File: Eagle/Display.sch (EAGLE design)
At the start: 79 parts, among them Q0A 310mA/60V/1.6Ω, Q0B 310mA/60V/1.6Ω, Q0C 310mA/60V/1.6Ω, Q10 310mA/60V/1.6Ω, Q11 310mA/60V/1.6Ω, Q12 310mA/60V/1.6Ω, Q13 310mA/60V/1.6Ω, Q14 310mA/60V/1.6Ω, Q15 310mA/60V/1.6Ω, Q16 310mA/60V/1.6Ω, Q17 310mA/60V/1.6Ω, Q18 310mA/60V/1.6Ω, Q19 310mA/60V/1.6Ω, Q1A 310mA/60V/1.6Ω, Q1B 310mA/60V/1.6Ω, Q1C 310mA/60V/1.6Ω, Q20 310mA/60V/1.6Ω, Q21 310mA/60V/1.6Ω, Q22A 310mA/60V/1.6Ω, Q22B 310mA/60V/1.6Ω, Q22C 310mA/60V/1.6Ω, Q22D 310mA/60V/1.6Ω, Q23 310mA/60V/1.6Ω, Q24 310mA/60V/1.6Ω, Q25 310mA/60V/1.6Ω, Q26 310mA/60V/1.6Ω, Q2A 310mA/60V/1.6Ω, Q2B 310mA/60V/1.6Ω, Q2C 310mA/60V/1.6Ω, Q3A 310mA/60V/1.6Ω, Q3B 310mA/60V/1.6Ω, Q3C 310mA/60V/1.6Ω, Q4A 310mA/60V/1.6Ω, Q4B 310mA/60V/1.6Ω, Q4C 310mA/60V/1.6Ω, Q5A 310mA/60V/1.6Ω, Q5B 310mA/60V/1.6Ω, Q5C 310mA/60V/1.6Ω, Q6A 310mA/60V/1.6Ω, Q6B 310mA/60V/1.6Ω, Q6C 310mA/60V/1.6Ω, Q7A 310mA/60V/1.6Ω, Q7B 310mA/60V/1.6Ω, Q7C 310mA/60V/1.6Ω, Q8A 310mA/60V/1.6Ω, Q8B 310mA/60V/1.6Ω, Q8C 310mA/60V/1.6Ω, Q9A 310mA/60V/1.6Ω, Q9B 310mA/60V/1.6Ω

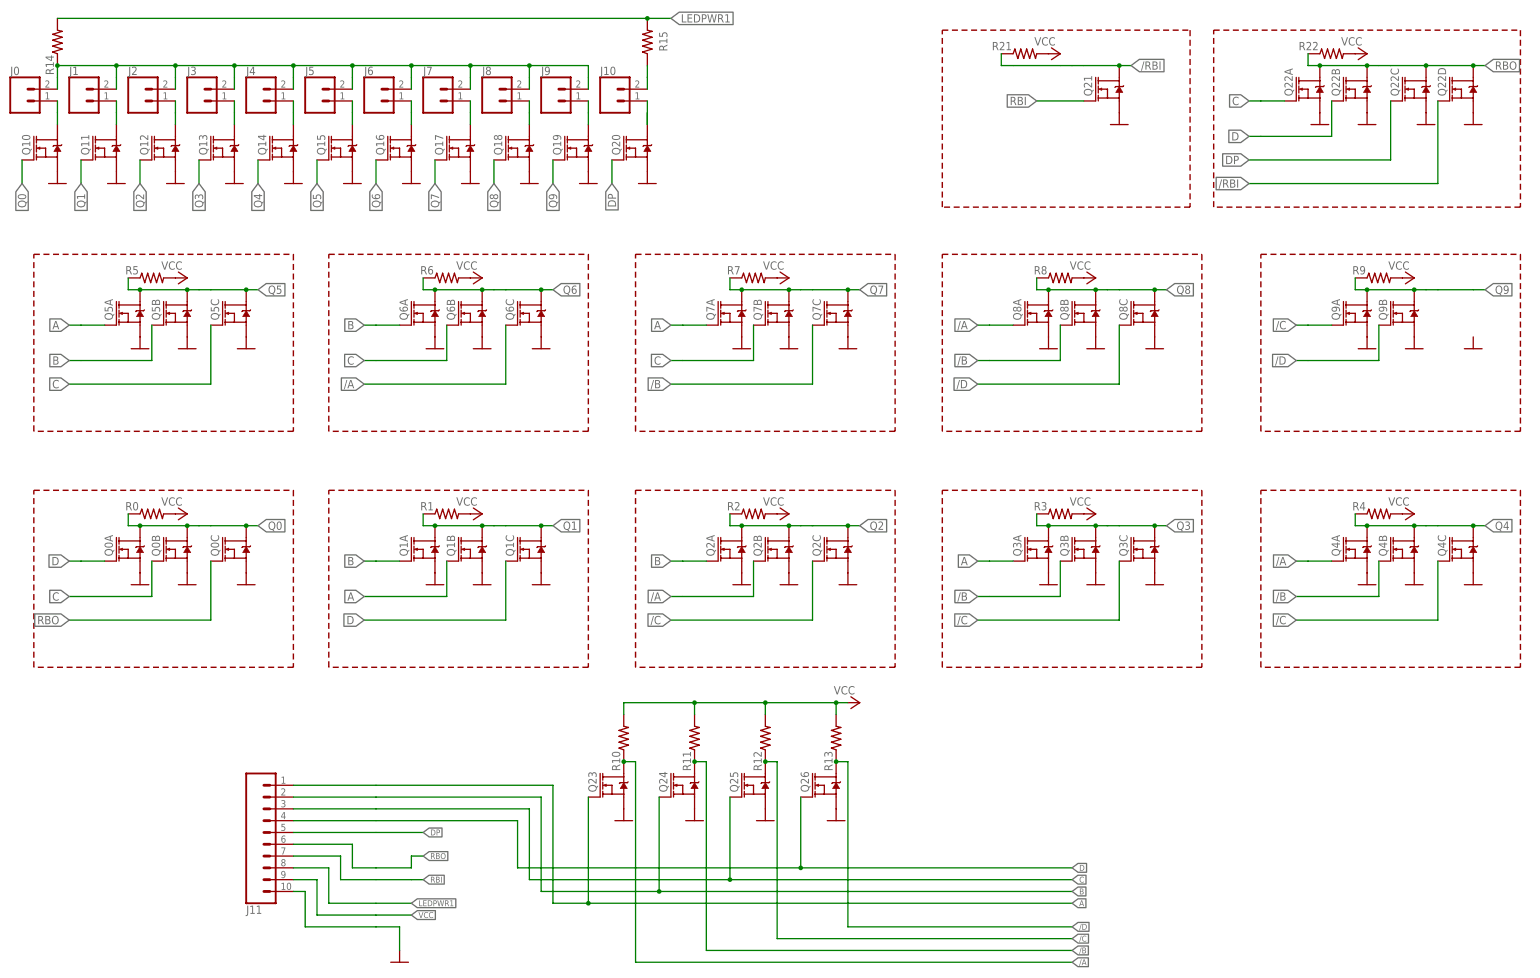
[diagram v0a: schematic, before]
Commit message: Rerouted for SOT23
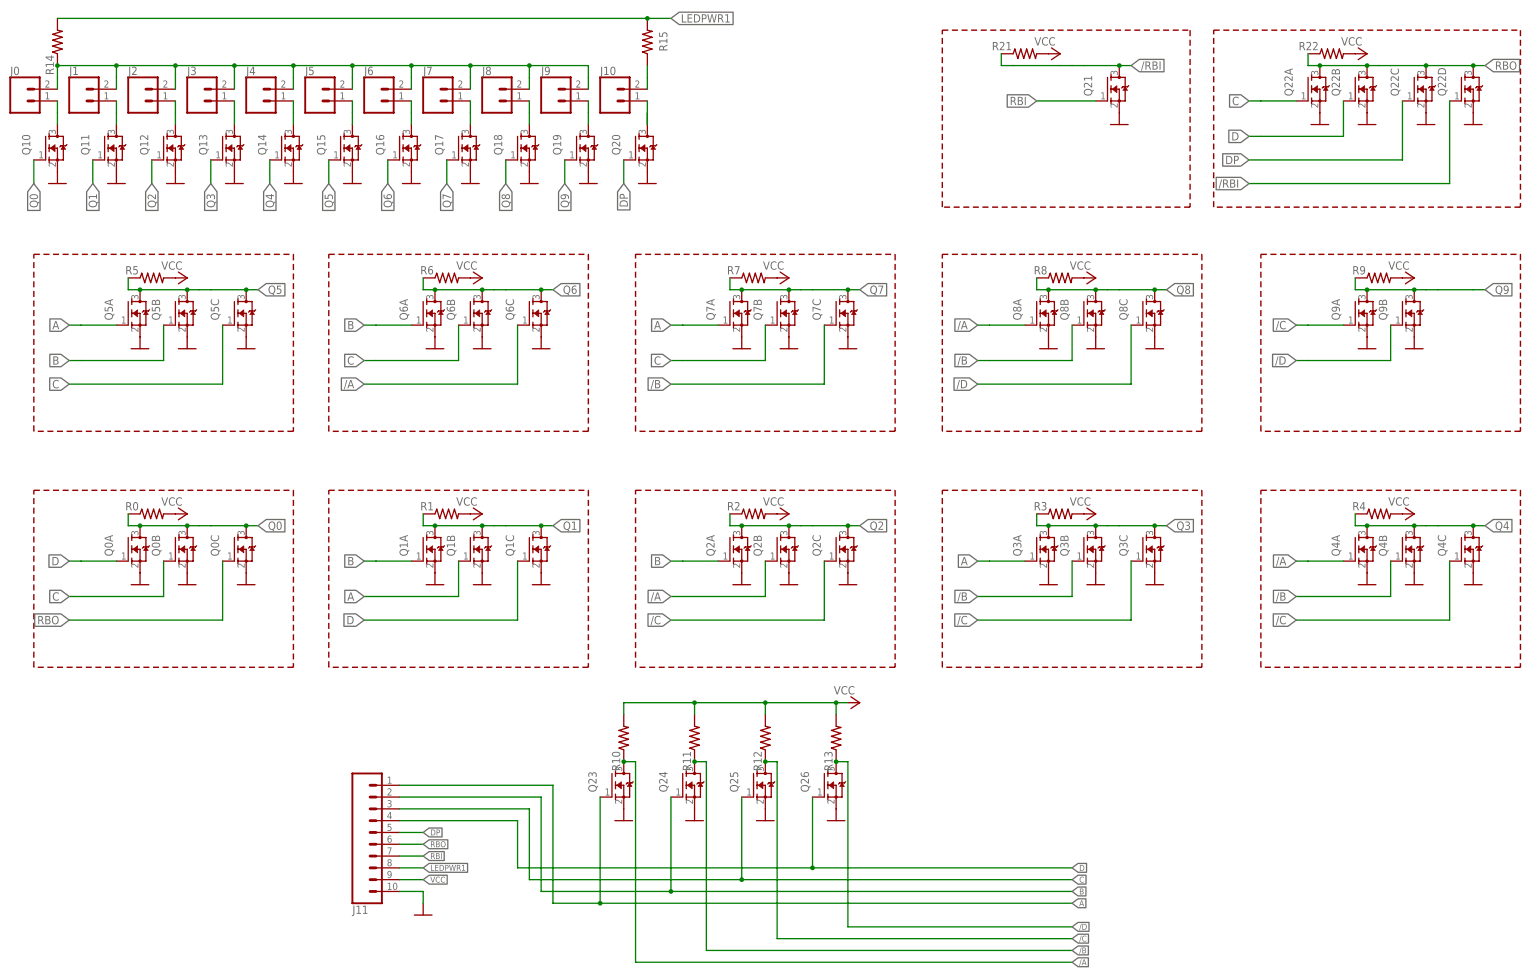
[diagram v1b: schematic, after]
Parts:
- Q0A, Q0B, Q0C, Q10, Q11, Q12, Q13, Q14, Q15, Q16, Q17, Q18, Q19, Q1A, Q1B, Q1C, Q20, Q21, Q22A, Q22B, Q22C, Q22D, Q23, Q24, Q25, Q26, Q2A, Q2B, Q2C, Q3A, Q3B, Q3C, Q4A, Q4B, Q4C, Q5A, Q5B, Q5C, Q6A, Q6B, Q6C, Q7A, Q7B, Q7C, Q8A, Q8B, Q8C, Q9A, Q9B: device SparkFun-DiscreteSemi:MOSFET-NCH-2N7002PW -> XSNOR:NMOSREFLOW
- R0, R1, R10, R11, R12, R13, R14, R15, R2, R21, R22, R3, R4, R5, R6, R7, R8, R9: device SparkFun-Resistors:RESISTOR0805 -> XSNOR:RESISTOR0805
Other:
- note added: "/A/B/C"
- note added: "/A/B/D"
- note added: "/C/D"
- note added: "A/B/C"
- note added: "ABC"
- note added: "AC/B"
- note added: "B/A/C"
- note added: "BAD"
- note added: "BC/A"
- note added: "CDDp/Rbi"
- note added: "DCRbo"
- note added: "Rbi -- /Rbi"
- moved on the sheet: J11

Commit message: Cleanups of PCBs
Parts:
- removed J11: (no value), SparkFun-Connectors:CONN_10"
- added JP1: (no value), XSNOR:PINHD-1X10/90
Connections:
- net A: now also JP1.1; no longer J11.1
- net B: now also JP1.2; no longer J11.2
- net C: now also JP1.3; no longer J11.3
- net D: now also JP1.4; no longer J11.4
- net DP: now also JP1.5; no longer J11.5
- net GND: now also JP1.10; no longer J11.10
- net LEDPWR1: now also JP1.8; no longer J11.8
- net RBI: now also JP1.7; no longer J11.7
- net RBO: now also JP1.6; no longer J11.6
- net VCC: now also JP1.9; no longer J11.9
